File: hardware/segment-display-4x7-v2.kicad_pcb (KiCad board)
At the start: 2 copper layers, 65 x 25 mm, 30 parts, among them P1 CON-SENSOR2, P2 DEBUG, P3 BOOT, U1 XMC1XXX24, U2 TM1637, U3 SEGMENT_4X7, U4 DRILL, U5 DRILL, U6 DRILL, U7 DRILL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

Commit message: Add layout
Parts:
- added G***: LOGO, kicad-libraries:Logo_CoMCU, B.Cu at (88.4, 42.3)
- moved Fiducial_Mark 49.6 mm to (100.4, 50.3)
- moved Fiducial_Mark 43.8 mm to (100.4, 31.3)
- moved Fiducial_Mark 13.2 mm to (64.4, 34.3)
- moved P3 6.81 mm to (65.9, 52.7)
- moved VAL 3.00 mm to (75.4, 42.3)
- moved VAL 1.32 mm to (62.4, 42.3)
- moved P2 0.62 mm to (54.3, 51.0)
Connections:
- U1 pad 13: Net-(U1-Pad13) -> Net-(P3-Pad2)
- U1 pad 4: Net-(P3-Pad2) -> Net-(U1-Pad4)
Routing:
- net +5V: track 12.7 -> 49.4 mm, vias 2 -> 6
- net Net-(P3-Pad2): track 0.00 -> 14.1 mm, vias 0 -> 2
- net VCC: track 32.1 -> 45.5 mm, vias 2 -> 4
- net Net-(R1-Pad1): track 0.00 -> 9.35 mm, vias 0 -> 2
- net GND: track 22.5 -> 24.6 mm, vias 12 -> 13
- net Net-(P2-Pad1): track 0.00 -> 1.47 mm

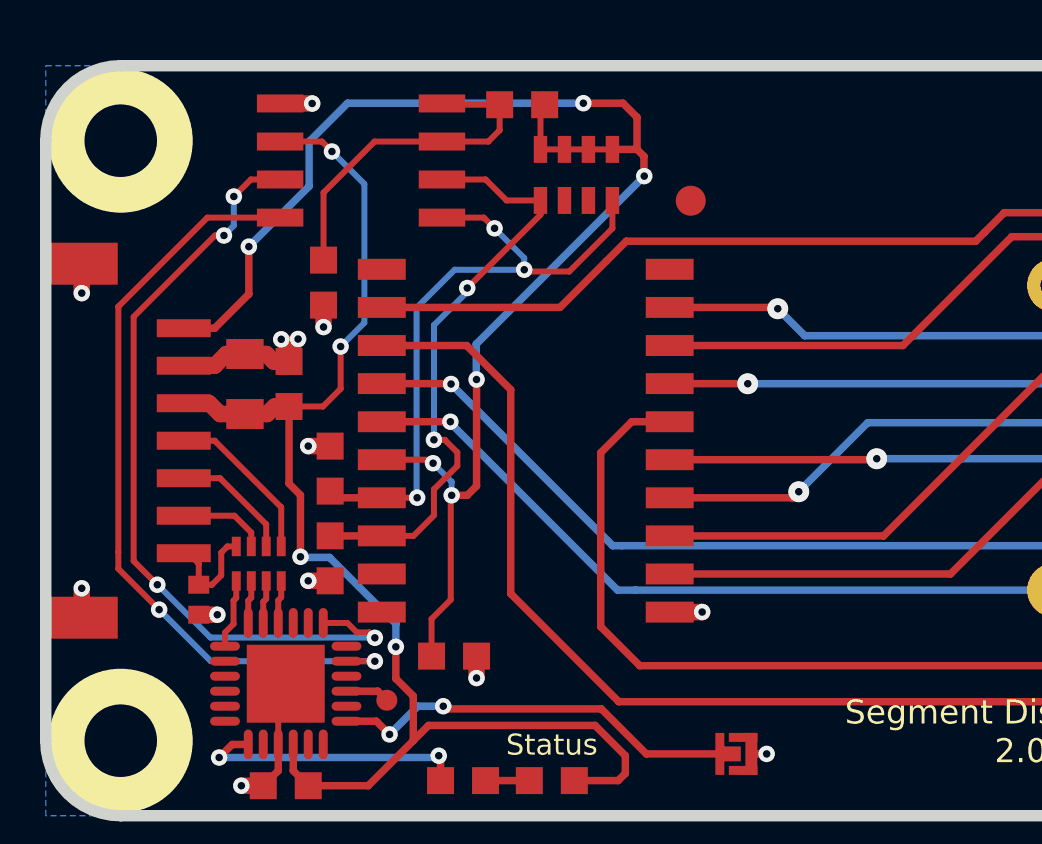
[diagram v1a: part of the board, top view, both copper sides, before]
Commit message: Add pullup resistors and change existing footprint to 4X0402
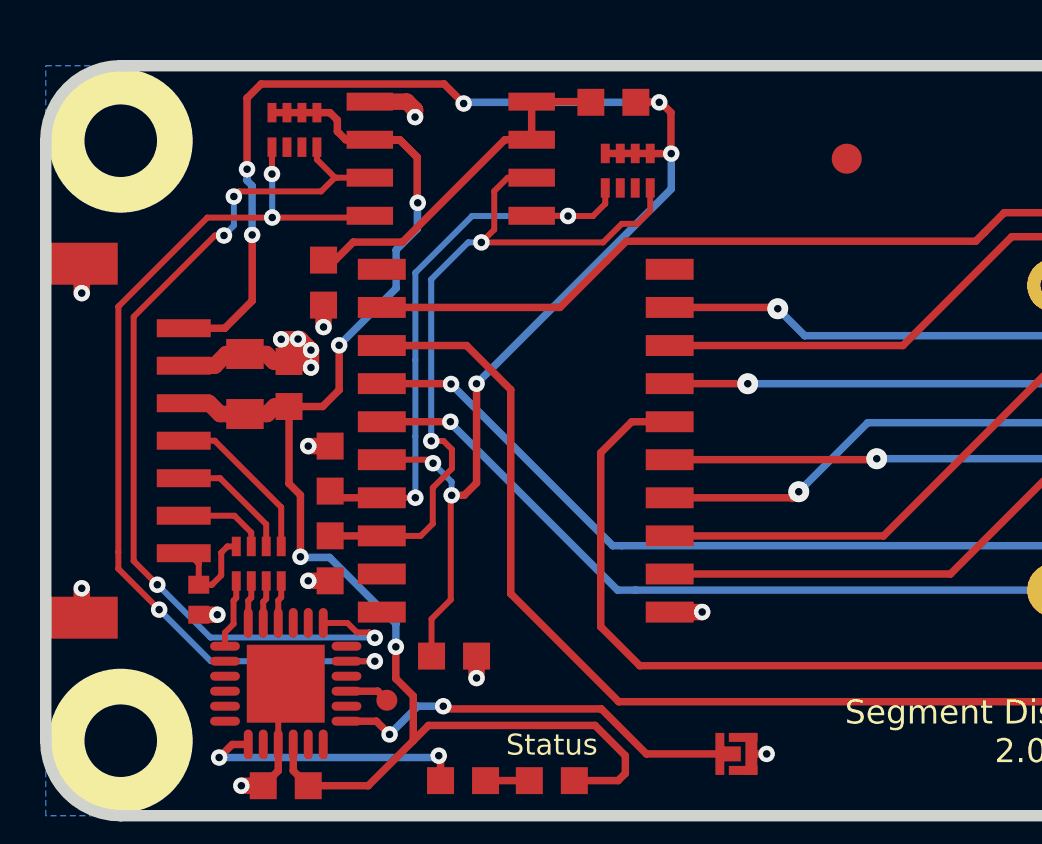
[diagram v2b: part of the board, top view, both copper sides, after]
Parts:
- added RP3: 2k2, kicad-libraries:4X0402, F.Cu at (51.2, 31.9)
- RP2: value 4k7 -> 2k2; footprint kicad-libraries:4X0603 -> kicad-libraries:4X0402
- moved Fiducial_Mark 5.39 mm to (69.6, 32.9)
- moved R2 3.04 mm to (61.8, 31.0)
- moved U8 2.99 mm to (56.4, 32.9)
- moved RP2 1.72 mm to (62.3, 33.3), turned to 180 degrees
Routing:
- net VCC: track 45.5 -> 51.2 mm
- net SDA: track 26.1 -> 31.5 mm, vias 2 -> 4
- net SCL2: track 20.1 -> 24.9 mm
- net SCL: track 26.5 -> 30.9 mm
- net GND: track 24.6 -> 28.4 mm, vias 13 -> 15
- net +5V: track 49.4 -> 52.1 mm, vias 6 -> 8
- net SDA2: track 21.6 -> 19.5 mm, vias 3 -> 2
